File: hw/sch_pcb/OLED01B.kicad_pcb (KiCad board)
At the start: 2 copper layers, 60.8 x 70.9 mm, 33 parts, among them J1 HEADER_2x03_PARALLEL, J2 HEADER_2x04_PARALLEL, J3 HEADER_1x03, J4 HEADER_2x05_PARALLEL, U1 MAX5026

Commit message: Update schematics
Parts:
- added U2: TLV840, Package_TO_SOT_SMD:SOT-23-5, F.Cu at (127.6, 82.3)
- added U3: PCA9306DP, Package_SO:TSSOP-8_3x3mm_P0.65mm, F.Cu at (155.8, 48.5)
- C1: renamed from C4; value 22uF -> 2.2uF
- C2: renamed from C1; value 4.7 uF -> 10uF
- D2: renamed from D1; value 15MQ040N -> 1A 20V 15MQ040N
- L1: value 4,7uH -> 4.7uH
- R9: renamed from R8; value 84k5 -> 100R
- renumbered C3 to C4, C6 to C5, C2 to C6, C5 to C7, D2 to D1, R7 to R1, R12 to R11, R11 to R12, R1 to R2, R2 to R3, R3 to R4, R4 to R5, R9 to R6, R5 to R7, R6 to R8
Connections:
- C2 pad 1: +3V3 -> +5V
- C4 pad 1: +3V3 -> +5V
- C5 pad 1: +3V3 -> +5V
- D1 pad 1: +3V3 -> +5V
- J1 pad 3: +3V3 -> +5V
- J1 pad 4: +3V3 -> +5V
- J4 pad 3: /D1 -> /SDAIN
- J4 pad 4: /D1 -> /SDAIN
- J4 pad 5: +3V3 -> +5V
- J4 pad 6: +3V3 -> +5V
- J4 pad 7: /CLK -> /SCLIN
- J4 pad 8: /CLK -> /SCLIN
- L1 pad 1: +3V3 -> +5V
- R13 pad 1: +3V3 -> +5V
- R13 pad 2: /D1 -> /SDAIN
- R14 pad 1: +3V3 -> +5V
- R14 pad 2: /CLK -> /SCLIN
- R6 pad 1: +3V3 -> /#RES
- R6 pad 2: /#RES -> +3V3
- U1 pad 4: +3V3 -> +5V
- U1 pad 5: +3V3 -> +5V
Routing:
- net +5V: track 0.00 -> 87.0 mm
- net +3V3: track 87.0 -> 0.00 mm
- net GND: vias 26 -> 27
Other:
- board text added: "GND SCL VCC SDA G"
- board text added: "GND SDA VCC SCL GND"
- board text removed: "GND CLK 3v3 SDA G"
- board text removed: "GND SDA 3v3 CLK GND"
- board text removed: "max. 3v3"

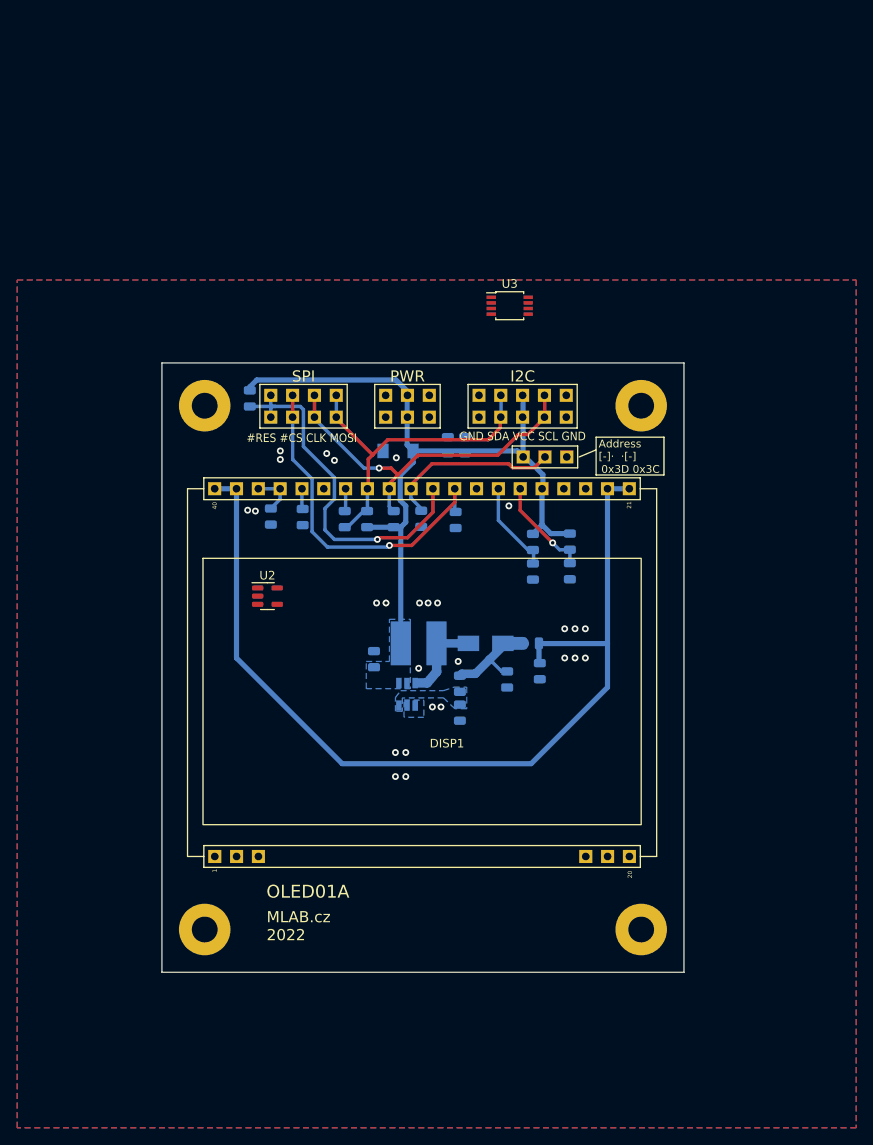
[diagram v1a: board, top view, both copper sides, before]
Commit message: add LDO type, fill packages, pcb placement
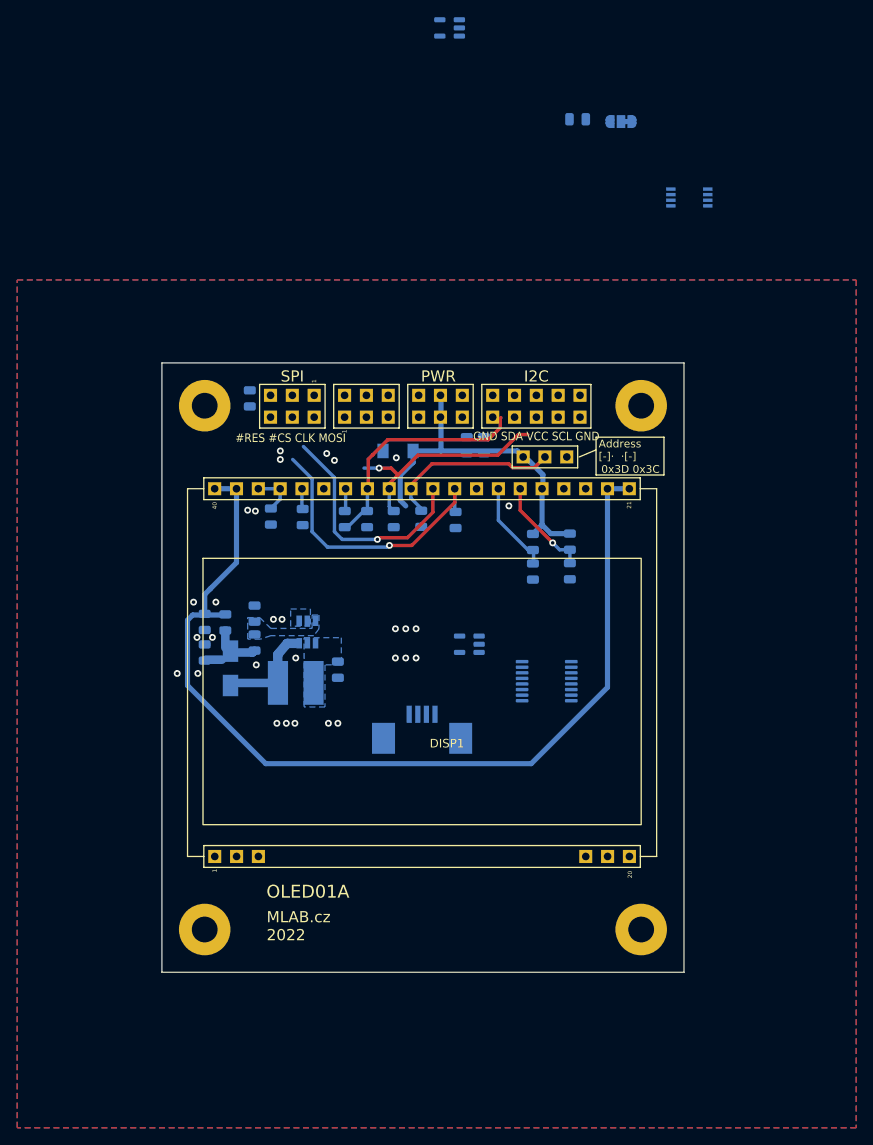
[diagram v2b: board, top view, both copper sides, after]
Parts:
- added C1: C_Small, Capacitor_SMD:C_0805_2012Metric, B.Cu at (163.7, 26.8)
- added J1: Conn_01x04_Male, Connector_FFC-FPC:TE_84952-4_1x04-1MP_P1.0mm_Horizontal, B.Cu at (145.6, 97.8)
- added J3: HEADER_2x03_PARALLEL, Mlab_Pin_Headers:Straight_2x03, F.Cu at (139.1, 60.2)
- added JP1: SolderJumper_3_Bridged12, Jumper:SolderJumper-3_P1.3mm_Bridged12_RoundedPad1.0x1.5mm, B.Cu at (168.8, 27.1)
- added U2: MIC5504-2.5YM5, Package_TO_SOT_SMD:SOT-23-5, B.Cu at (148.8, 16.2)
- added U4: TSC2007, Package_SO:TSSOP-16_4.4x5mm_P0.65mm, B.Cu at (160.1, 92.2)
- J4: renamed from J2; value HEADER_2x04_PARALLEL -> HEADER_2x03_PARALLEL; footprint Mlab_Pin_Headers:Straight_2x04 -> Mlab_Pin_Headers:Straight_2x03
- U1: renamed from U2; moved to B.Cu
- U5: renamed from U3; moved to B.Cu
- moved C11 39.4 mm to (120.3, 85.3)
- moved R9 35.6 mm to (122.7, 85.4), turned to 90 degrees
- moved C10 35.3 mm to (120.3, 88.9), turned to 90 degrees
- moved D1 29.8 mm to (123.3, 90.7), turned to -90 degrees
- moved R8 26.5 mm to (126.1, 84.3), turned to 90 degrees
- moved U5 24.4 mm to (176.7, 35.9), turned to 180 degrees
- moved R7 24.4 mm to (126.1, 87.7), turned to 90 degrees
- moved U1 24.2 mm to (151.1, 87.9), turned to 180 degrees
- moved L1 15.0 mm to (130.9, 92.4), turned to 180 degrees
- moved U3 13.7 mm to (132.3, 86.5), turned to -90 degrees
- moved C5 4.37 mm to (135.8, 90.9), turned to -90 degrees
- moved J2 3.84 mm to (147.7, 60.2)
- moved C8 2.20 mm to (152.8, 64.7)
- moved C9 2.20 mm to (150.8, 64.7)
- moved J6 1.60 mm to (158.9, 60.2)
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- renumbered C6 to C10, C7 to C11, C1 to C2, C2 to C5, C4 to C8, C5 to C9, D2 to D1, D1 to D2, J1 to J2, J3 to J5, J4 to J6, U1 to U3
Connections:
- net +3V3 renamed +2V5
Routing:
- net +5V: track 87.0 -> 40.4 mm
- net /CLK: track 41.6 -> 0.00 mm, vias 1 -> 0
- net /D1: track 38.0 -> 0.00 mm
- net /SDAIN: track 0.00 -> 27.0 mm
- net /SCLIN: track 0.00 -> 25.6 mm, vias 0 -> 1
- net /#RES: track 42.6 -> 27.3 mm
- net /#CS: track 40.5 -> 33.2 mm
- net Net-(C10-Pad1): track 11.7 -> 5.79 mm
- net +12V: track 110.2 -> 113.0 mm
- net Net-(D1-Pad2): track 9.73 -> 11.7 mm
- net GND: vias 27 -> 29
- added copper zone on B.Cu, net +5V
- removed copper zone on B.Cu, net +2V5

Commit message: WIP
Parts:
- moved U2 100.1 mm to (149.0, 116.3)
- moved JP1 93.1 mm to (155.2, 119.2)
- moved U5 80.2 mm to (157.4, 113.7)
- moved C1 45.6 mm to (169.4, 72.0)
- moved U1 23.2 mm to (169.8, 74.2)
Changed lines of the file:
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@@
     (pad "6" smd rect locked (at 1.31 0.95 270) (size 1.22 0.65) (layers "B.Cu" "B.Paste" "B.Mask")
       (net 18 "Net-(D1-Pad2)") (pinfunction "LX") (pintype "unspecified"))
-    (model "${KISYS3DMOD}/Package_TO_SOT_SMD.3dshapes/TSOT-23-6.wrl"
+    (model "${KICAD6_3DMODEL_DIR}/Package_TO_SOT_SMD.3dshapes/TSOT-23-6.wrl"
       (offset (xyz 0 0 0))
       (scale (xyz 1 1 1))
@@
   )
   (footprint "Package_TO_SOT_SMD:SOT-23-5" (layer "B.Cu")
-    (at 148.8 16.17 180)
+    (at 149 116.3 180)
     (descr "SOT, 5 Pin (https://www.jedec.org/sites/default/files/docs/Mo-178c.PDF variant AA), generated with kicad-footprint-generator ipc_gullwing_generator.py")
     (tags "SOT TO_SOT_SMD")
@@
   )
   (footprint "Package_SO:TSSOP-8_3x3mm_P0.65mm" (layer "B.Cu")
-    (at 176.7 35.9 180)
+    (at 157.4 113.7 180)
     (descr "TSSOP8: plastic thin shrink small outline package; 8 leads; body width 3 mm; (see NXP SSOP-TSSOP-VSO-REFLOW.pdf and sot505-1_po.pdf)")
     (tags "SSOP 0.65")
@@
   )
   (footprint "Jumper:SolderJumper-3_P1.3mm_Bridged12_RoundedPad1.0x1.5mm" (layer "B.Cu")
-    (at 168.75 27.07 180)
+    (at 155.2 119.2 180)
     (descr "SMD Solder 3-pad Jumper, 1x1.5mm rounded Pads, 0.3mm gap, pads 1-2 bridged with 1 copper strip")
     (tags "net tie solder jumper bridged")
@@
   )
   (footprint "Capacitor_SMD:C_0805_2012Metric" (layer "B.Cu")
-    (at 163.7 26.8 180)
+    (at 169.45 72 180)
     (descr "Capacitor SMD 0805 (2012 Metric), square (rectangular) end terminal, IPC_7351 nominal, (Body size source: IPC-SM-782 page 76, https://www.pcb-3d.com/wordpress/wp-content/uploads/ipc-sm-782a_amendment_1_and_2.pdf, https://docs.google.com/spreadsheets/d/1BsfQQcO9C6DZCsRaXUlFlo91Tg2WpOkGARC1WS5S8t0/edit?usp=sharing), generated with kicad-footprint-generator")
     (tags "capacitor")
@@
   )
   (footprint "Package_TO_SOT_SMD:SOT-23-5" (layer "B.Cu")
-    (at 151.1 87.9 180)
+    (at 169.8375 74.25 180)
     (descr "SOT, 5 Pin (https://www.jedec.org/sites/default/files/docs/Mo-178c.PDF variant AA), generated with kicad-footprint-generator ipc_gullwing_generator.py")
     (tags "SOT TO_SOT_SMD")
